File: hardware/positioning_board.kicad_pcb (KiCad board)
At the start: 2 copper layers, 83 x 43 mm, 50 parts, among them J1 Conn_01x04, J2 Conn_01x05, J3 Conn_01x05, J4 4P4C, J5 USB_C_Receptacle_USB2.0_16P, Q1 MMBT3904, Q2 MMBT3904, SW1 SW_Push, SW2 SW_Push, U1 AMS1117-3.3, U2 ESP32-S3-WROOM-1, U3 LSM6DS3, U4 SN65HVD1782DR, U5 TPS563200, U6 CH340K

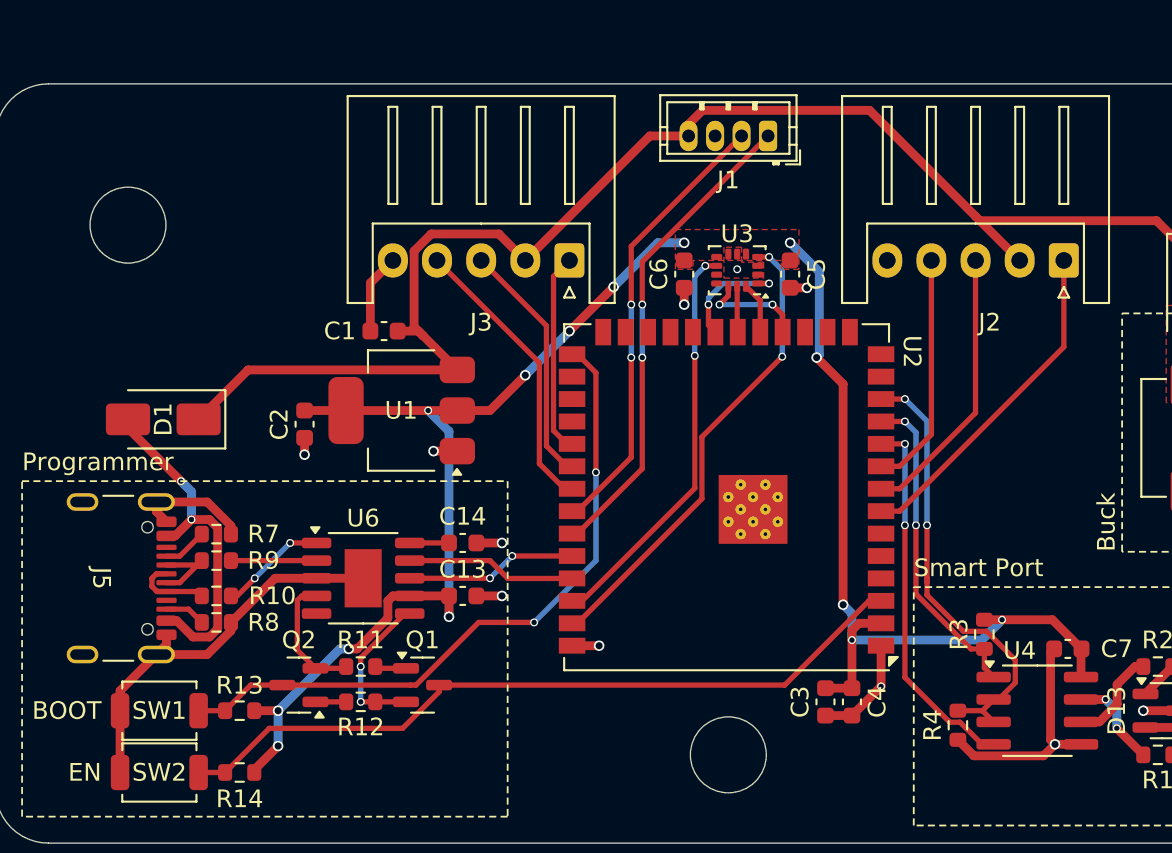
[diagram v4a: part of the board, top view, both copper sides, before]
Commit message: swap lidar and brain UART channels
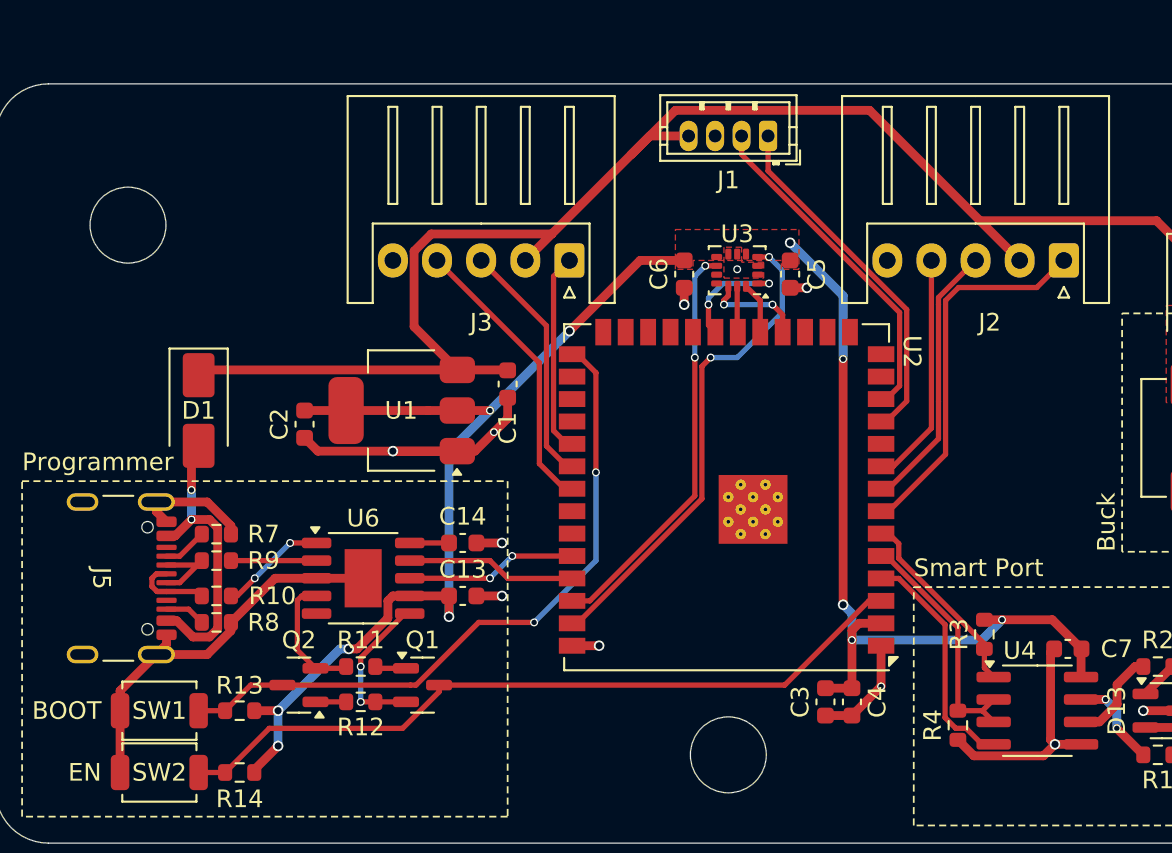
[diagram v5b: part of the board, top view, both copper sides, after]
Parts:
- moved C1 7.62 mm to (127.5, 84.0), turned to 90 degrees
- moved D1 2.06 mm to (110.0, 85.5), turned to -90 degrees
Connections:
- U2 pad 10: /Brain_TX -> unconnected-(U2-IO17-Pad10)
- U2 pad 11: /Brain_RX -> /LIDAR_RX
- U2 pad 12: /Brain_Dir -> /LIDAR_PWM
- U2 pad 34: /LIDAR_PWM -> unconnected-(U2-IO41-Pad34)
- U2 pad 35: /LIDAR_RX -> unconnected-(U2-IO42-Pad35)
- U2 pad 4: unconnected-(U2-IO4-Pad4) -> /Brain_TX
- U2 pad 5: unconnected-(U2-IO5-Pad5) -> /Brain_Dir
- U2 pad 6: unconnected-(U2-IO6-Pad6) -> /Brain_RX
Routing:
- net /Brain_Dir: track 25.8 -> 13.9 mm, vias 2 -> 0
- net GND: track 63.8 -> 74.4 mm
- net /Brain_TX: track 21.2 -> 13.3 mm, vias 2 -> 0
- net /Brain_RX: track 18.4 -> 11.0 mm, vias 2 -> 0
- net /LIDAR_RX: track 27.3 -> 20.2 mm, vias 2 -> 0
- net /LIDAR_PWM: track 25.4 -> 19.2 mm, vias 2 -> 0
- net +5V: track 81.1 -> 85.5 mm
- net /usb_port/+5V: track 19.8 -> 17.0 mm
- net /Encoder1_B: track 19.1 -> 21.3 mm
- net /IMU_INT1: track 26.8 -> 27.7 mm
- net +3V3: track 104.6 -> 104.5 mm, vias 14 -> 11

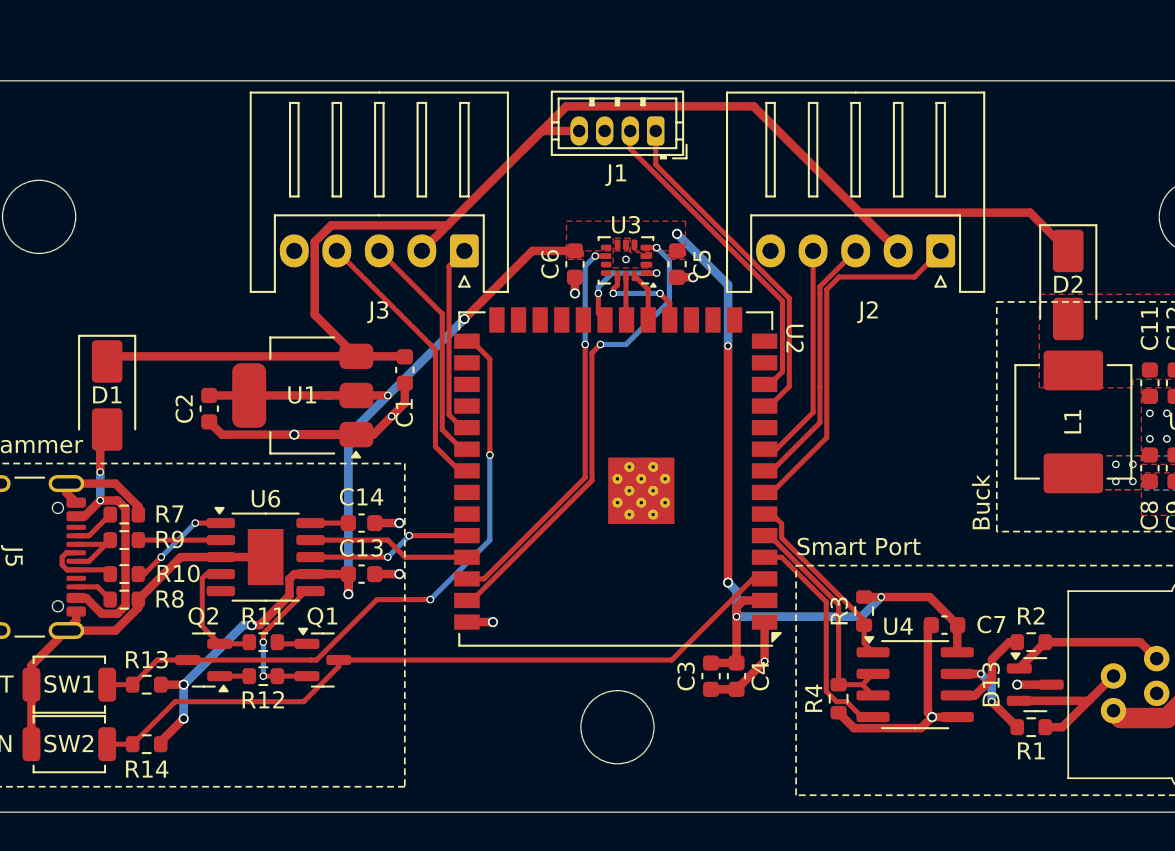
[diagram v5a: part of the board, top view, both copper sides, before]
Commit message: switch to 4 layer
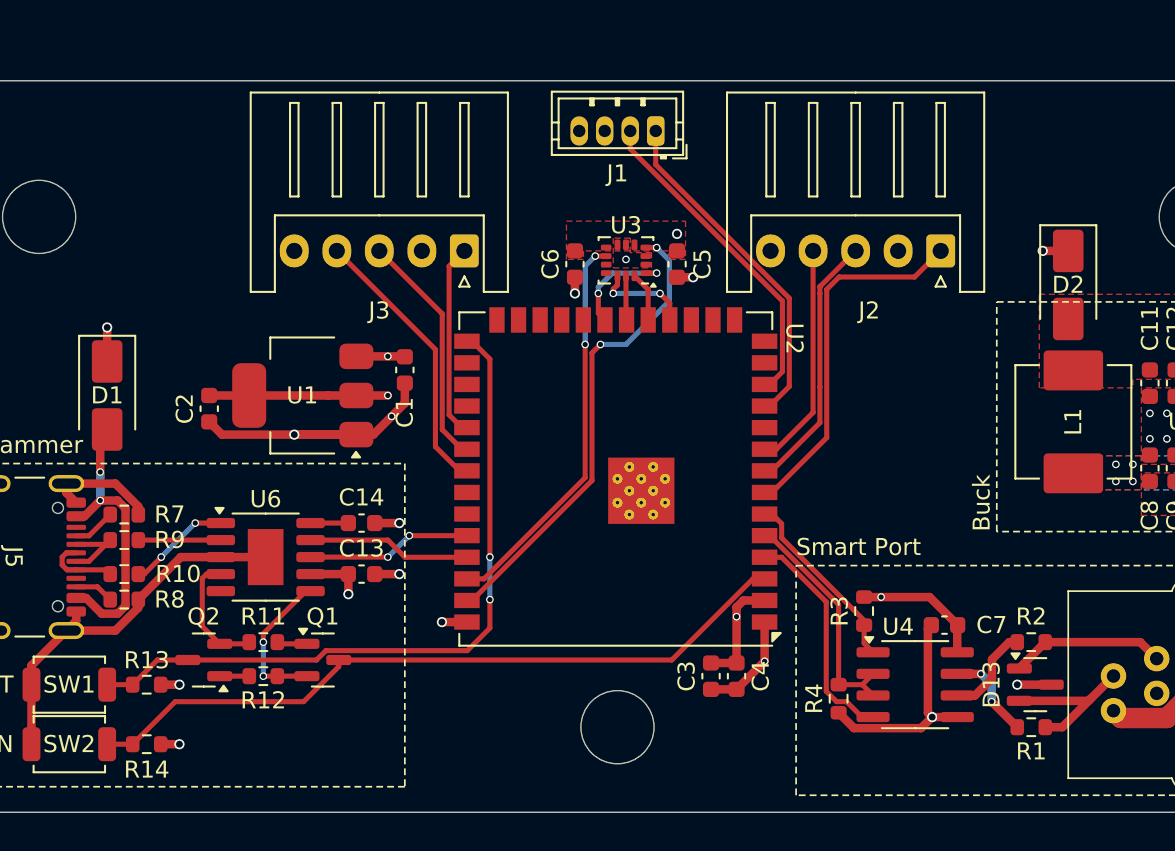
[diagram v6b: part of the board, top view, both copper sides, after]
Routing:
- net +5V: track 85.5 -> 6.78 mm, vias 0 -> 3
- net +3V3: track 104.5 -> 30.5 mm, vias 11 -> 7
- net /GPIO0: track 38.4 -> 41.5 mm
- added copper zone on In2.Cu, net +3V3
- added copper zone on In1.Cu, net +5V
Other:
- copper layers 2 -> 4

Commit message: optimize size
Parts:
- moved D2 11.7 mm to (158.5, 87.5), turned to 90 degrees
- moved J2 4.72 mm to (163.0, 79.5)
- moved J3 4.72 mm to (127.0, 79.5)
- moved C7 3.16 mm to (156.2, 98.0)
- moved D13 3.16 mm to (161.6, 101.5)
- moved J4 3.16 mm to (171.0, 101.5)
- moved R1 3.16 mm to (161.3, 104.0)
- moved R2 3.16 mm to (161.3, 99.0)
- moved R3 3.16 mm to (151.5, 97.2)
- moved R4 3.16 mm to (150.0, 102.3)
- moved U4 3.16 mm to (154.5, 101.5)
- moved J1 3.00 mm to (142.2, 73.0)
- moved C10 2.83 mm to (173.2, 87.5)
- moved L1 2.83 mm to (164.0, 87.5)
- moved R5 2.83 mm to (172.3, 84.5)
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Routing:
- net /12V_Buck/+12V: track 26.5 -> 23.3 mm
- net /LIDAR_RX: track 20.2 -> 17.2 mm
- net /Encoder2_X: track 16.4 -> 19.2 mm
- net /usb_port/+5V: track 17.0 -> 19.6 mm
- net /Brain_TX: track 13.3 -> 11.1 mm
- net /Brain_Dir: track 13.9 -> 11.8 mm
- net /MCU_EN: track 42.9 -> 40.9 mm
- net /GPIO0: track 41.5 -> 39.5 mm
- net /Prog_TX: track 9.61 -> 7.61 mm
- net /Prog_RX: track 9.72 -> 7.72 mm
- net /LIDAR_PWM: track 19.2 -> 17.3 mm
- net /Encoder2_A: track 14.0 -> 15.7 mm
- net /Encoder2_B: track 11.4 -> 9.86 mm
- net /Encoder1_B: track 21.3 -> 20.0 mm
- net /Encoder1_X: track 13.2 -> 12.3 mm
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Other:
- board size 83 x 43 mm -> 75 x 40 mm
- board text added: "IMU"

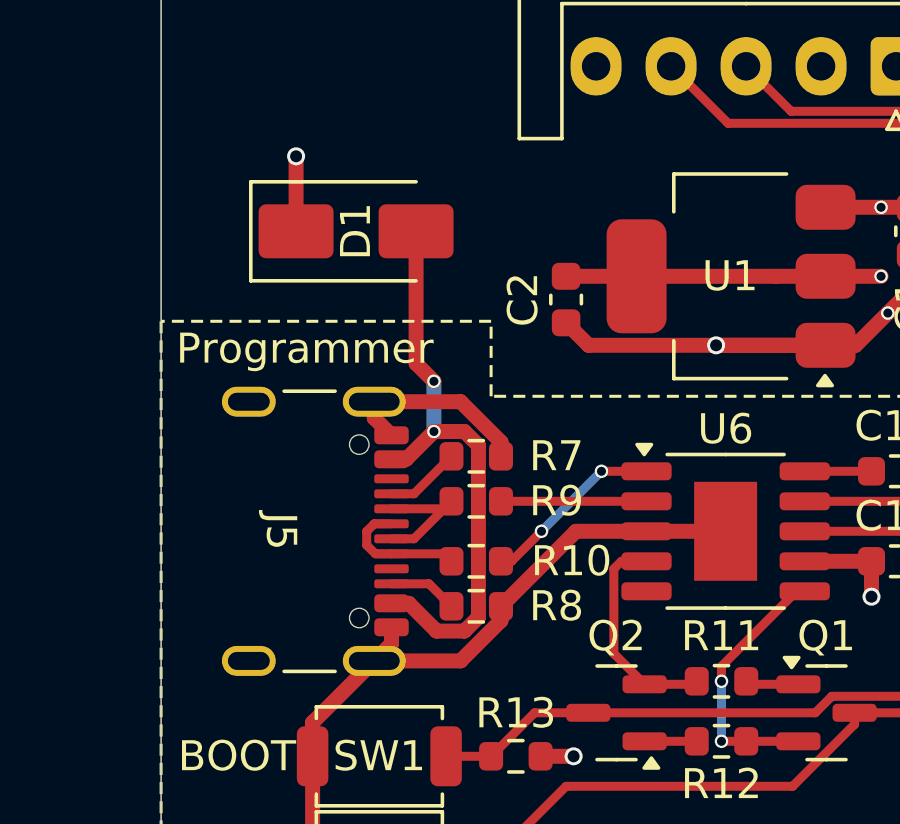
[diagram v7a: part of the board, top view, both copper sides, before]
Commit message: fix programmer differential routing
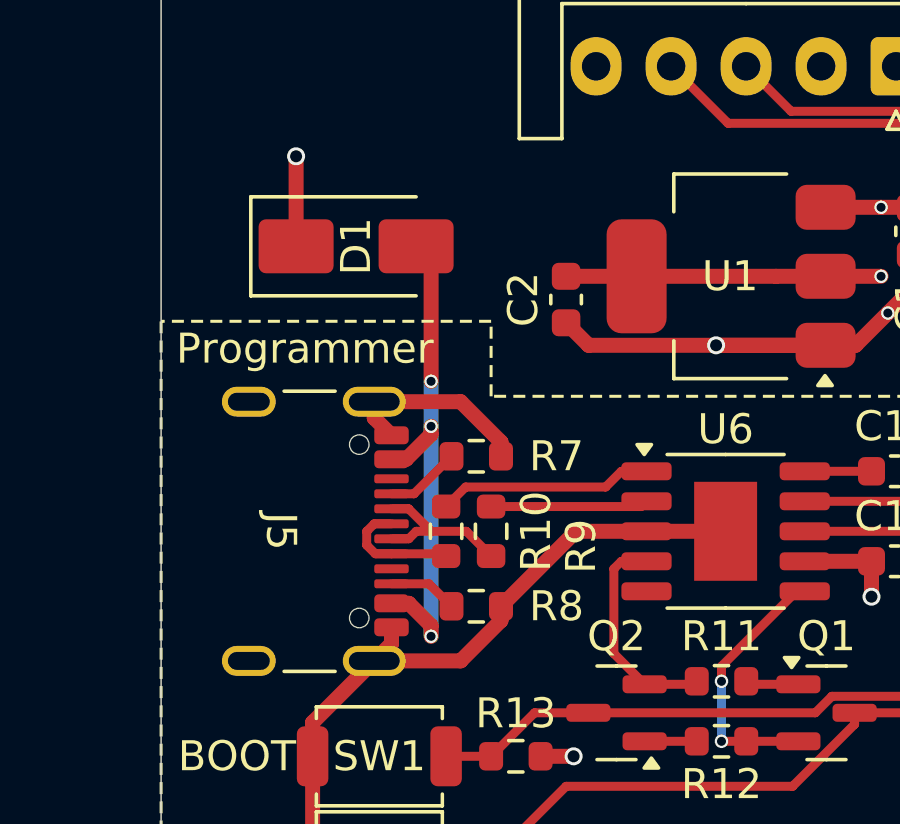
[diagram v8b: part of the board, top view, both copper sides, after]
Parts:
- moved R10 1.42 mm to (112.0, 95.0), turned to 90 degrees
- moved R9 1.12 mm to (113.5, 95.0), turned to 90 degrees
- moved D1 0.50 mm to (109.0, 85.5)
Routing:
- net /usb_port/+5V: track 19.6 -> 17.1 mm, vias 2 -> 3
- net /usb_port/USB_D+: track 6.09 -> 7.17 mm, vias 2 -> 0
- net Net-(J5-D--PadA7): track 4.62 -> 5.40 mm
